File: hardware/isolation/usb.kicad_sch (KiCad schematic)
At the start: 27 parts, among them IC1 ISO6542DBQR, Q3 Si2365EDS, U2 FT230XS, U3 RI3-0505S

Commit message: sync
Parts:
- removed C18, C19: 1uF, Capacitor_SMD:C_0603_1608Metric, symbol Device:C_Small
- removed C52, C53: 22uF, Capacitor_SMD:C_0805_2012Metric, symbol Device:C_Small
- added C66, C67, C68, C69: 47uF, Capacitor_SMD:C_0805_2012Metric, symbol Device:C_Small
- C40, C51: value 22uF -> 100nF; footprint Capacitor_SMD:C_0805_2012Metric -> Capacitor_SMD:C_0603_1608Metric; Manufacturer_Name MCASH21GCC7684MTCA1J -> --; Manufacturer_Part_Number CL21A107MQYNNWE -> --; Mouser Part Number 810-C2012X5R1V226MAC -> --; Mouser Price/Stock (none) -> https://www.mouser.pl/ProductDetail/KEMET/C0603C104J3RACTU?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
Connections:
- net +3.3VISO: now also C51.2
- net +3.3VUSB: now also C40.2
- net +5VUSBISO: now also C66.1, C67.1; no longer C40.2, C51.2
- net GNDISO: now also C66.2, C67.2; no longer C40.1
- net GNDUSB: now also C40.1, C68.2, C69.2
- net TXD: now also IC1.5 (OUTC); no longer IC1.12 (OUTC)
- net _TXD: now also IC1.12 (INC); no longer IC1.5 (INC)
- net at L2.1, U3.2 (+VIN): now also C68.1
- net at C35.2, L2.2, Q3.3 (D): now also C69.1
- net VCC: now reaches C44.1, FB7.1, U2.12 (VCC)

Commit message: pcb finished
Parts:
- added D18: 5.3V/400W, Package_TO_SOT_SMD:SOT-23-3, symbol Power_Protection:ESDA5V3L
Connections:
- net GNDUSB: now also D18.3 (A)
- net at R18.2, U2.8 (USBDP): now also D18.2 (K)
- net at R15.1, U2.9 (USBDM): now also D18.1 (K)
- net +3.3VISO renamed +3.3VIOISO
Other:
- moved on the sheet: R15, R18

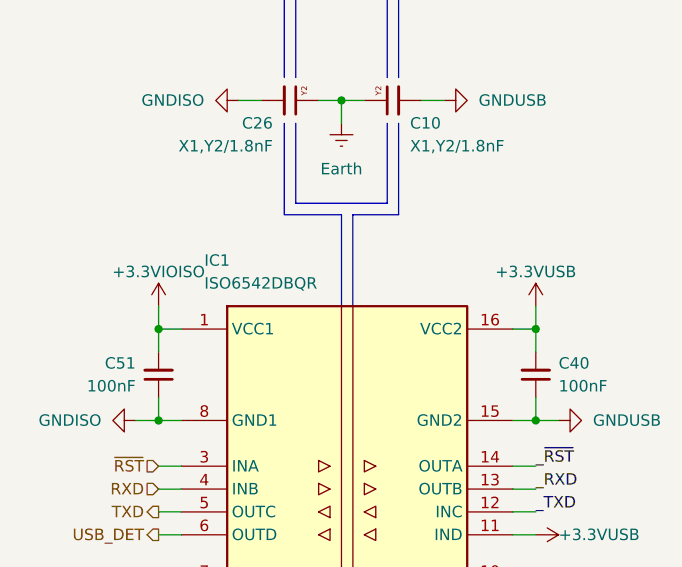
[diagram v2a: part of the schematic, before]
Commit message: relay fix and changed ic PN for isolated rx/tx for usb to a type with standard output low instead of high
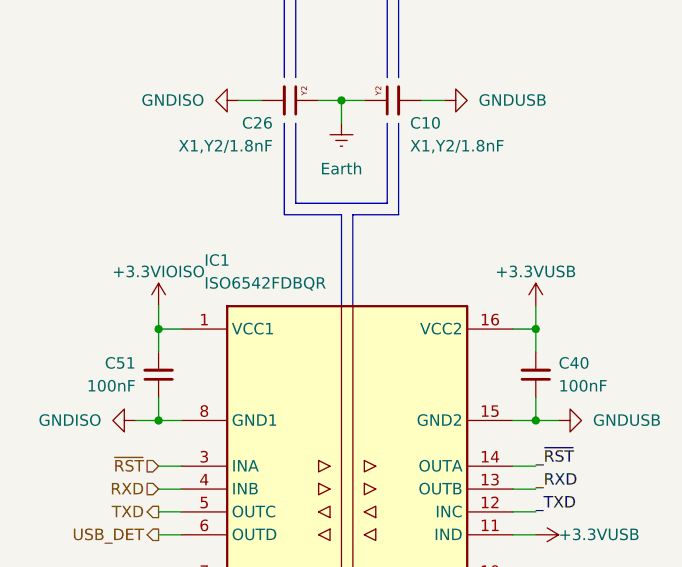
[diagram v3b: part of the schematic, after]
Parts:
- IC1: value ISO6542DBQR -> ISO6542FDBQR; Manufacturer_Part_Number ISO6542DBQR -> ISO6542FDBQR; Mouser Part Number 595-ISO6542DBQR -> 595-ISO6542FDBQR; Mouser Price/Stock https://www.mouser.pl/ProductDetail/Texas-Instruments/ISO6542DBQR?qs=2FehpBK1j961cqatM6gsZg%3D%3D -> https://www.mouser.pl/ProductDetail/Texas-Instruments/ISO6542FDBQR?qs=2FehpBK1j95VNOtIBfXh0A%3D%3D
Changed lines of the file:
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@@
 			)
 		)
-		(property "Value" "ISO6542DBQR"
+		(property "Value" "ISO6542FDBQR"
 			(at 60.96 116.84 0)
 			(show_name no)
@@
 			)
 		)
-		(property "Datasheet" "https://www.ti.com/lit/ds/symlink/iso6542.pdf?ts=1774362260370&ref_url=https%253A%252F%252Fwww.mouser.es%252F"
+		(property "Datasheet" "https://www.ti.com/lit/ds/symlink/iso6542.pdf?ts=1777813802072&ref_url=https%253A%252F%252Fwww.mouser.pl%252F"
 			(at 105.41 327 0)
 			(hide yes)
@@
 			)
 		)
-		(property "Mouser Part Number" "595-ISO6542DBQR"
+		(property "Mouser Part Number" "595-ISO6542FDBQR"
 			(at 105.41 627 0)
 			(hide yes)
@@
 			)
 		)
-		(property "Mouser Price/Stock" "https://www.mouser.pl/ProductDetail/Texas-Instruments/ISO6542DBQR?qs=2FehpBK1j961cqatM6gsZg%3D%3D"
+		(property "Mouser Price/Stock" "https://www.mouser.pl/ProductDetail/Texas-Instruments/ISO6542FDBQR?qs=2FehpBK1j95VNOtIBfXh0A%3D%3D"
 			(at 105.41 727 0)
 			(hide yes)
@@
 			)
 		)
-		(property "Manufacturer_Part_Number" "ISO6542DBQR"
+		(property "Manufacturer_Part_Number" "ISO6542FDBQR "
 			(at 105.41 927 0)
 			(hide yes)

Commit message: sync
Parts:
- removed C35: 100nF, Capacitor_SMD:C_0603_1608Metric, symbol Device:C_Small
- removed Q3: Si2365EDS, Package_TO_SOT_SMD:SOT-23-3, symbol Transistor_FET:Q_PMOS_GSD
- removed R80: 1k, Resistor_SMD:R_0603_1608Metric, symbol Device:R_Small
- removed R81: 100k, Resistor_SMD:R_0603_1608Metric, symbol Device:R_Small
- added R76: 0, Resistor_SMD:R_0603_1608Metric, symbol Device:R_Small
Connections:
- net +5VUSB: now also C69.1, L2.2
- net _~{RST}: now also R76.2; no longer IC1.14 (OUTA)
- new net: IC1.14 (OUTA), R76.1
